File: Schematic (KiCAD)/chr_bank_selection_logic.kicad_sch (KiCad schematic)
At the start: 70 parts, among them X10 INVERT, X11 Reg 1 DFF-No-Reset N

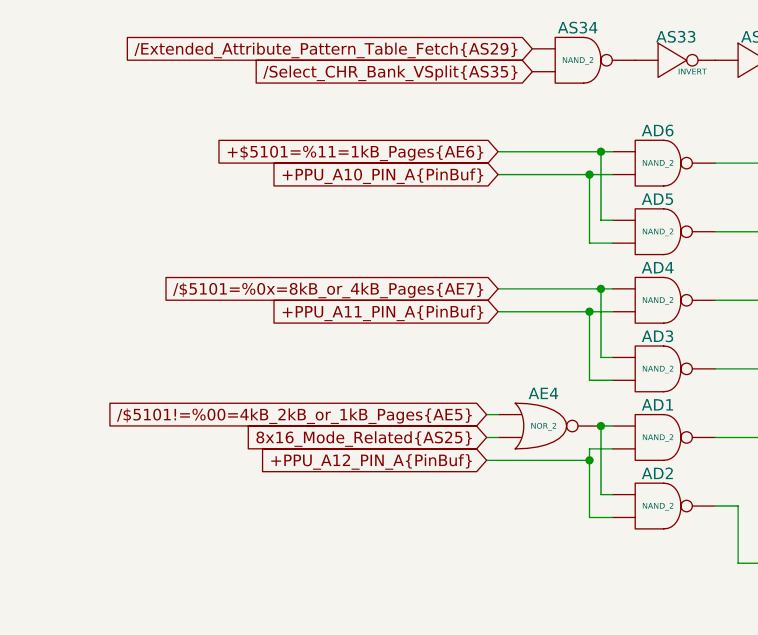
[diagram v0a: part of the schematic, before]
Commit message: Tracing and schematic updates.  - Added timer to schematic.  - Added all items from artifacts sheet to the MMC5A trace.
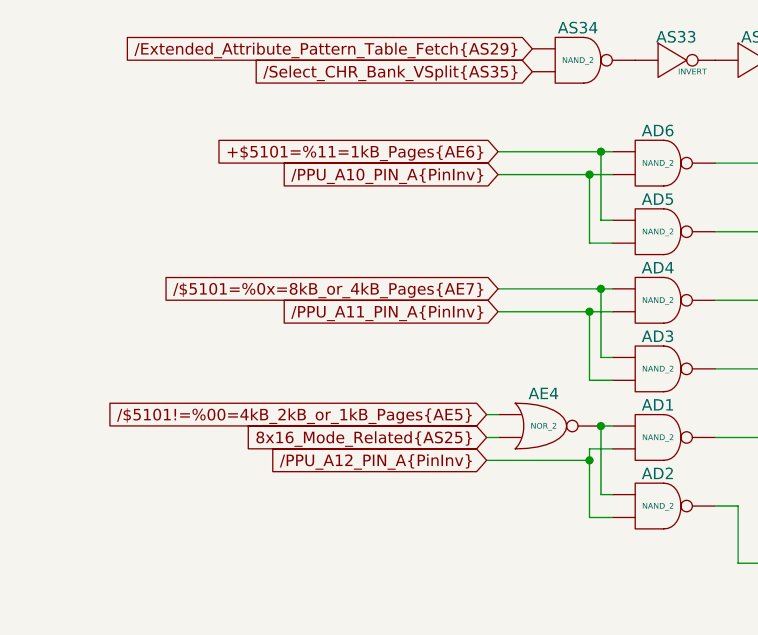
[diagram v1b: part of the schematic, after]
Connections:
- net +PPU_A10_PIN_A{PinBuf} is gone; now on net /PPU_A10_PIN_A{PinInv}: AD5. (X), AD6. (X)
- net +PPU_A11_PIN_A{PinBuf} is gone; now on net /PPU_A11_PIN_A{PinInv}: AD3. (X), AD4. (X)
- net +PPU_A12_PIN_A{PinBuf} is gone; now on net /PPU_A12_PIN_A{PinInv}: AD1. (X), AD2. (X)
- net at AD8. (/Y7): now also AD5. (X); no longer AD3. (X)
- net at AS33. (X): now also AS4. (X); no longer AS34. (X)
- net at AD7. (/Y7): now also AS16. (X); no longer AS14. (X)
- net /PPU_A10_PIN_A{PinInv}: now reaches AD6. (X)
- net /PPU_A10_PIN_A{PinInv}: no longer AD7. (/Y7)
- net /PPU_A12_PIN_A{PinInv}: now reaches AD1. (X), AD2. (X)
- net /PPU_A12_PIN_A{PinInv}: no longer AE4. (X)
- net /PPU_A11_PIN_A{PinInv}: now reaches AD4. (X)
- net /PPU_A11_PIN_A{PinInv}: no longer AD7. (/Y7)
- net at X10. (X): now also AS26. (X), AS27. (X); no longer X11. (/Q0)
- new net: AD3. (X), AD8. (/Y7)
- new net: AD8. (/Y7), AS1. (X), AS2. (X), AS3. (X), AS9. (X)
- new net: AS33. (X), AS34. (X)
- new net: AS29. (X), AS30. (X)
- new net: AT3. (X), AT4. (X)
- new net: AD10. (X), AD9. (X), AS4. (X)
- new net: AD8. (/Y7), AS21. (X), AS8. (X)
- new net: AD7. (/Y7), AS14. (X)
- new net: AD7. (/Y7), AS18. (X)
- new net: AD8. (/Y7), AS17. (X), AS6. (X), AS7. (X)
- new net: AD8. (/Y7), AS23. (X)
- new net: AD6. (X), AD7. (/Y7)
- new net: AS38. (X), AT2. (X)
- new net: AD1. (X), AD2. (X), AE4. (X)
- new net: AD2. (X), AD8. (/Y7)
- new net: AD4. (X), AD7. (/Y7)
- new net: X10. (X), X11. (/Q0)
- new net: AD7. (/Y7), AS20. (X)
- new net: AD7. (/Y7), AS12. (X)
- new net: AS27. (X), AS28. (X)
- new net: AS25. (X), AS27. (X), AS28. (X)
- new net: AS25. (X), AS26. (X)
- new net: AD8. (/Y7), AS13. (X), AS5. (X)
- new net: AD8. (/Y7), AS11. (X)
- new net: AD1. (X), AD7. (/Y7)
- new net: AD8. (/Y7), AS15. (X)
- new net: AD8. (/Y7), AS19. (X)
- new net: AD7. (/Y7), AS10. (X)
- new net: AD7. (/Y7), AS22. (X)
- new net: AD7. (/Y7), AS24. (X)
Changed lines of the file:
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@@
 		)
 	)
-	(global_label "+PPU_A12_PIN_A{PinBuf}"
+	(global_label "{slash}PPU_A12_PIN_A{PinInv}"
 		(shape input)
 		(at 58.42 64.77 180)
@@
 		)
 		(property "Intersheetrefs" "${INTERSHEET_REFS}"
-			(at 31.4257 64.77 0)
+			(at 32.0909 64.77 0)
 			(effects
 				(font
@@
 		)
 	)
-	(global_label "+PPU_A10_PIN_A{PinBuf}"
+	(global_label "{slash}PPU_A10_PIN_A{PinInv}"
 		(shape input)
 		(at 59.69 33.02 180)
@@
 		)
 		(property "Intersheetrefs" "${INTERSHEET_REFS}"
-			(at 32.6957 33.02 0)
+			(at 33.3609 33.02 0)
 			(effects
 				(font
@@
 		)
 	)
-	(global_label "+PPU_A11_PIN_A{PinBuf}"
+	(global_label "{slash}PPU_A11_PIN_A{PinInv}"
 		(shape input)
 		(at 59.69 48.26 180)
@@
 		)
 		(property "Intersheetrefs" "${INTERSHEET_REFS}"
-			(at 32.6957 48.26 0)
-			(effects
-				(font
+			(at 33.3609 48.26 0)
+			(effects
+				(font

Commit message: - Updated all of the various And-OR-Invert gates to have consistent names.  - Added the schematic for CL3 / SL3 GPIO pins.  There are no surprises revealed by this.  - Finished up the CPU address decoding tracing.  - Added one of the 'artifact' counters from the pulse channels
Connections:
- net at AD8. (/Y7): now also AD5. (X); no longer AD3. (X)
- net at AS33. (X): now also AS4. (X); no longer AS34. (X)
- net at AD7. (/Y7): now also AS16. (X); no longer AS14. (X)
- net at X10. (X): now also AS26. (X), AS27. (X); no longer X11. (/Q0)
- new net: AD3. (X), AD8. (/Y7)
- new net: AD8. (/Y7), AS1. (X), AS2. (X), AS3. (X), AS9. (X)
- new net: AS33. (X), AS34. (X)
- new net: AS29. (X), AS30. (X)
- new net: AT3. (X), AT4. (X)
- new net: AD10. (X), AD9. (X), AS4. (X)
- new net: AD8. (/Y7), AS21. (X), AS8. (X)
- new net: AD7. (/Y7), AS14. (X)
- new net: AD7. (/Y7), AS18. (X)
- new net: AD8. (/Y7), AS17. (X), AS6. (X), AS7. (X)
- new net: AD8. (/Y7), AS23. (X)
- new net: AD6. (X), AD7. (/Y7)
- new net: AS38. (X), AT2. (X)
- new net: AD1. (X), AD2. (X), AE4. (X)
- new net: AD2. (X), AD8. (/Y7)
- new net: AD4. (X), AD7. (/Y7)
- new net: X10. (X), X11. (/Q0)
- new net: AD7. (/Y7), AS20. (X)
- new net: AD7. (/Y7), AS12. (X)
- new net: AS27. (X), AS28. (X)
- new net: AS25. (X), AS27. (X), AS28. (X)
- new net: AS25. (X), AS26. (X)
- new net: AD8. (/Y7), AS13. (X), AS5. (X)
- new net: AD8. (/Y7), AS11. (X)
- new net: AD1. (X), AD7. (/Y7)
- new net: AD8. (/Y7), AS15. (X)
- new net: AD8. (/Y7), AS19. (X)
- new net: AD7. (/Y7), AS10. (X)
- new net: AD7. (/Y7), AS22. (X)
- new net: AD7. (/Y7), AS24. (X)
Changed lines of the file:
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@@
 	)
 	(symbol
-		(lib_name "INVERT_20")
 		(lib_id "MMC5:INVERT")
 		(at 255.27 181.61 0)
@@
 	)
 	(symbol
-		(lib_name "NAND_2_2")
+		(lib_name "NAND_2_3")
 		(lib_id "MMC5:NAND_2")
 		(at 77.47 54.61 0)
@@
 	)
 	(symbol
-		(lib_name "NOR_2_1")
+		(lib_name "NOR_2_6")
 		(lib_id "MMC5:NOR_2")
 		(at 134.62 154.94 0)
@@
 	)
 	(symbol
-		(lib_name "BUFFER_1")
 		(lib_id "MMC5:BUFFER")
 		(at 267.97 186.69 0)
@@
 	)
 	(symbol
-		(lib_name "NAND_3_14")
 		(lib_id "MMC5:NAND_3")
 		(at 266.7 153.67 0)
@@
 	)
 	(symbol
-		(lib_name "INVERT_19")
+		(lib_name "INVERT_4")
 		(lib_id "MMC5:INVERT")
 		(at 269.24 205.74 0)
@@
 	)
 	(symbol
-		(lib_name "INVERT_30")
+		(lib_name "INVERT_28")
 		(lib_id "MMC5:INVERT")
 		(at 269.24 83.82 0)
@@
 	)
 	(symbol
-		(lib_name "INVERT_2")
+		(lib_name "INVERT_24")
 		(lib_id "MMC5:INVERT")
 		(at 97.79 17.78 0)
@@
 	)
 	(symbol
-		(lib_name "NOR_2_3")
 		(lib_id "MMC5:NOR_2")
 		(at 134.62 85.09 0)
@@
 	)
 	(symbol
-		(lib_name "INVERT_17")
+		(lib_name "INVERT_1")
 		(lib_id "MMC5:INVERT")
 		(at 134.62 50.8 0)
@@
 	)
 	(symbol
-		(lib_name "INVERT_15")
+		(lib_name "INVERT_7")
 		(lib_id "MMC5:INVERT")
 		(at 134.62 43.18 0)
@@
 	)
 	(symbol
+		(lib_name "NOR_2_1")
 		(lib_id "MMC5:NOR_2")
 		(at 134.62 105.41 0)
@@
 	)
 	(symbol
-		(lib_name "NAND_2_4")
+		(lib_name "NAND_2_5")
 		(lib_id "MMC5:NAND_2")
 		(at 77.47 31.75 0)
@@
 	)
 	(symbol
-		(lib_name "NAND_2_9")
+		(lib_name "NAND_2_14")
 		(lib_id "MMC5:NAND_2")
 		(at 257.81 48.26 0)
@@
 	)
 	(symbol
-		(lib_name "INVERT_32")
+		(lib_name "INVERT_30")
 		(lib_id "MMC5:INVERT")
 		(at 269.24 96.52 0)
@@
 	)
 	(symbol
-		(lib_name "INVERT_21")
+		(lib_name "INVERT_6")
 		(lib_id "MMC5:INVERT")
 		(at 269.24 166.37 0)
@@
 	)
 	(symbol
-		(lib_name "INVERT_27")
+		(lib_name "INVERT_26")
 		(lib_id "MMC5:INVERT")
 		(at 80.01 20.32 0)
@@
 	)
 	(symbol
-		(lib_name "INVERT_8")
+		(lib_name "INVERT_13")
 		(lib_id "MMC5:INVERT")
 		(at 134.62 99.06 0)
@@
 	)
 	(symbol
-		(lib_name "NOR_2_7")
+		(lib_name "NOR_2_2")
 		(lib_id "MMC5:NOR_2")
 		(at 257.81 195.58 0)
@@
 	)
 	(symbol
-		(lib_name "NAND_2_3")
+		(lib_name "NAND_2_2")
 		(lib_id "MMC5:NAND_2")
 		(at 77.47 69.85 0)
@@
 	)
 	(symbol
-		(lib_name "INVERT_22")
+		(lib_name "INVERT_23")
 		(lib_id "MMC5:INVERT")
 		(at 97.79 24.13 0)
@@
 	)
 	(symbol
-		(lib_name "INVERT_29")
+		(lib_name "INVERT_27")
 		(lib_id "MMC5:INVERT")
 		(at 269.24 58.42 0)
@@
 	)
 	(symbol
-		(lib_name "NAND_3_4")
+		(lib_name "NAND_3_5")
 		(lib_id "MMC5:NAND_3")
 		(at 257.81 119.38 0)
@@
 	)
 	(symbol
-		(lib_name "INVERT_14")
+		(lib_name "INVERT_8")
 		(lib_id "MMC5:INVERT")
 		(at 128.27 39.37 0)
@@
 	)
 	(symbol
-		(lib_name "NOR_2_6")
+		(lib_name "NOR_2_3")
 		(lib_id "MMC5:NOR_2")
 		(at 134.62 170.18 0)
@@
 	)
 	(symbol
-		(lib_name "NAND_2_15")
+		(lib_name "NAND_2_12")
 		(lib_id "MMC5:NAND_2")
 		(at 257.81 110.49 0)
@@
 	)
 	(symbol
-		(lib_name "NAND_3_13")
+		(lib_name "NAND_3_2")
 		(lib_id "MMC5:NAND_3")
 		(at 257.81 205.74 0)
@@
 	)
 	(symbol
-		(lib_name "INVERT_28")
+		(lib_name "INVERT_29")
 		(lib_id "MMC5:INVERT")
 		(at 269.24 53.34 0)
@@
 	)
 	(symbol
-		(lib_name "INVERT_4")
+		(lib_name "INVERT_11")
 		(lib_id "MMC5:INVERT")
 		(at 128.27 54.61 0)
@@
 	)
 	(symbol
+		(lib_name "NAND_2_1")
 		(lib_id "MMC5:NAND_2")
 		(at 123.19 228.6 0)
@@
 	)
 	(symbol
-		(lib_name "INVERT_3")
+		(lib_name "INVERT_14")
 		(lib_id "MMC5:INVERT")
 		(at 134.62 142.24 0)
@@
 	)
 	(symbol
-		(lib_name "NAND_3_1")
+		(lib_name "NAND_3_4")
 		(lib_id "MMC5:NAND_3")
 		(at 123.19 215.9 0)
@@
 	)
 	(symbol
-		(lib_name "NAND_2_13")
+		(lib_name "NAND_2_15")
 		(lib_id "MMC5:NAND_2")
 		(at 257.81 91.44 0)
@@
 	)
 	(symbol
-		(lib_name "NOR_2_5")
+		(lib_name "NOR_2_4")
 		(lib_id "MMC5:NOR_2")
 		(at 134.62 162.56 0)
@@
 	)
 	(symbol
-		(lib_name "NAND_2_14")
+		(lib_name "NAND_2_9")
 		(lib_id "MMC5:NAND_2")
 		(at 257.81 102.87 0)
@@
 	)
 	(symbol
-		(lib_name "INVERT_23")
+		(lib_name "INVERT_15")
 		(lib_id "MMC5:INVERT")
 		(at 255.27 148.59 0)
@@
 	)
 	(symbol
-		(lib_name "NAND_2_5")
+		(lib_name "NAND_2_4")
 		(lib_id "MMC5:NAND_2")
 		(at 77.47 62.23 0)
@@
 	)
 	(symbol
-		(lib_name "INVERT_25")
+		(lib_name "INVERT_9")
 		(lib_id "MMC5:INVERT")
 		(at 255.27 158.75 0)
@@
 	)
 	(symbol
-		(lib_name "INVERT_9")
+		(lib_name "INVERT_12")
 		(lib_id "MMC5:INVERT")
 		(at 134.62 120.65 0)
@@
 	)
 	(symbol
-		(lib_name "Decoder_3to8_1")
 		(lib_id "MMC5:Decoder_3to8")
 		(at 111.76 72.39 0)
@@
 	)
 	(symbol
-		(lib_name "NOR_2_2")
+		(lib_name "NOR_2_5")
 		(lib_id "MMC5:NOR_2")
 		(at 134.62 134.62 0)
@@
 	)
 	(symbol
-		(lib_name "INVERT_11")
+		(lib_name "INVERT_21")
 		(lib_id "MMC5:INVERT")
 		(at 134.62 148.59 0)
@@
 	)
 	(symbol
-		(lib_name "NAND_3_8")
+		(lib_name "NAND_3_1")
 		(lib_id "MMC5:NAND_3")
 		(at 257.81 217.17 0)
@@
 	)
 	(symbol
-		(lib_name "INVERT_18")
+		(lib_name "INVERT_16")
 		(lib_id "MMC5:INVERT")
 		(at 134.62 58.42 0)
@@
 	)
 	(symbol
-		(lib_name "INVERT_26")
+		(lib_name "INVERT_17")
 		(lib_id "MMC5:INVERT")
 		(at 246.38 148.59 0)
@@
 	)
 	(symbol
-		(lib_name "INVERT_13")
+		(lib_name "INVERT_20")
 		(lib_id "MMC5:INVERT")
 		(at 134.62 35.56 0)
@@
 	)
 	(symbol
-		(lib_name "NOR_2_4")
+		(lib_name "NOR_2_7")
 		(lib_id "MMC5:NOR_2")
 		(at 134.62 113.03 0)
@@
 	)
 	(symbol
-		(lib_name "INVERT_24")
+		(lib_name "INVERT_25")
 		(lib_id "MMC5:INVERT")
 		(at 88.9 20.32 0)
@@
 	)
 	(symbol
-		(lib_name "INVERT_7")
+		(lib_name "INVERT_18")
 		(lib_id "MMC5:INVERT")
 		(at 134.62 92.71 0)
@@
 	)
 	(symbol
+		(lib_name "BUFFER_1")
 		(lib_id "MMC5:BUFFER")
 		(at 267.97 195.58 0)
@@
 	)
 	(symbol
+		(lib_name "Decoder_3to8_1")
 		(lib_id "MMC5:Decoder_3to8")
 		(at 111.76 33.02 0)
@@
 	)
 	(symbol
-		(lib_name "INVERT_6")
+		(lib_name "INVERT_19")
 		(lib_id "MMC5:INVERT")
 		(at 134.62 78.74 0)
@@
 	)
 	(symbol
-		(lib_name "NAND_2_12")
+		(lib_name "NAND_2_13")
 		(lib_id "MMC5:NAND_2")
 		(at 257.81 71.12 0)
@@
 	)
 	(symbol
-		(lib_name "INVERT_12")
+		(lib_name "INVERT_2")
 		(lib_id "MMC5:INVERT")
 		(at 128.27 31.75 0)
@@
 	)
 	(symbol
-		(lib_name "INVERT_1")
+		(lib_name "INVERT_22")
 		(lib_id "MMC5:INVERT")
 		(at 69.85 218.44 0)
@@
 	)
 	(symbol
-		(lib_name "INVERT_16")
+		(lib_name "INVERT_3")
 		(lib_id "MMC5:INVERT")
 		(at 128.27 46.99 0)
@@
 	)
 	(symbol
-		(lib_name "NAND_2_1")
 		(lib_id "MMC5:NAND_2")
 		(at 77.47 39.37 0)
